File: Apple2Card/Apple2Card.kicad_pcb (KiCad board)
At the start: 2 copper layers, 160 x 78.2 mm, 77 parts, among them J1 ICSP, J2 Conn_01x25, J3 Conn_01x25, J4 Conn_01x16, J5 SERCON, J6 WIZNET 5500, SW1 SW_Push, U1 ATmega328P-P, U2 74HCT32, U3 74HCT00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

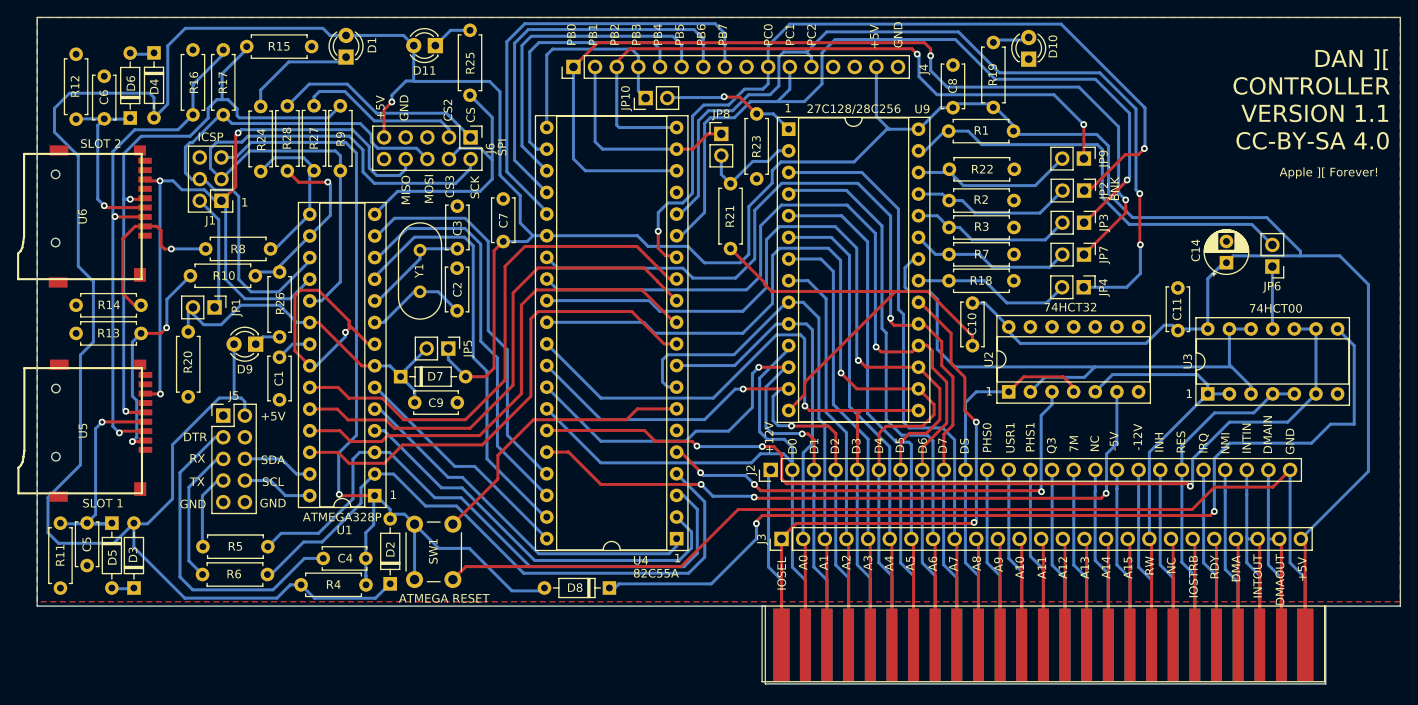
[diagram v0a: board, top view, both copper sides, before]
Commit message: Minor updates to PCB & schematics: - Realigned some components (LEDs etc). - Added some clearance to the slot connector (now allows production with "chamfered edges"). - Show component values on the silk screen (so no separate schematics are required when soldering) - Changed pull-down resistors for 82C55s I/O pins to 4k7 (instead of 10k), since they   were too weak to overcome the minimum current mentioned in the 8255 data sheet   (though the 10k resistors still worked with most types - but not with all). - Changed the two load resistors for the SD card supply voltage, to slightly increase the   voltage drop across the diodes. The SD supply voltage was a bit high.
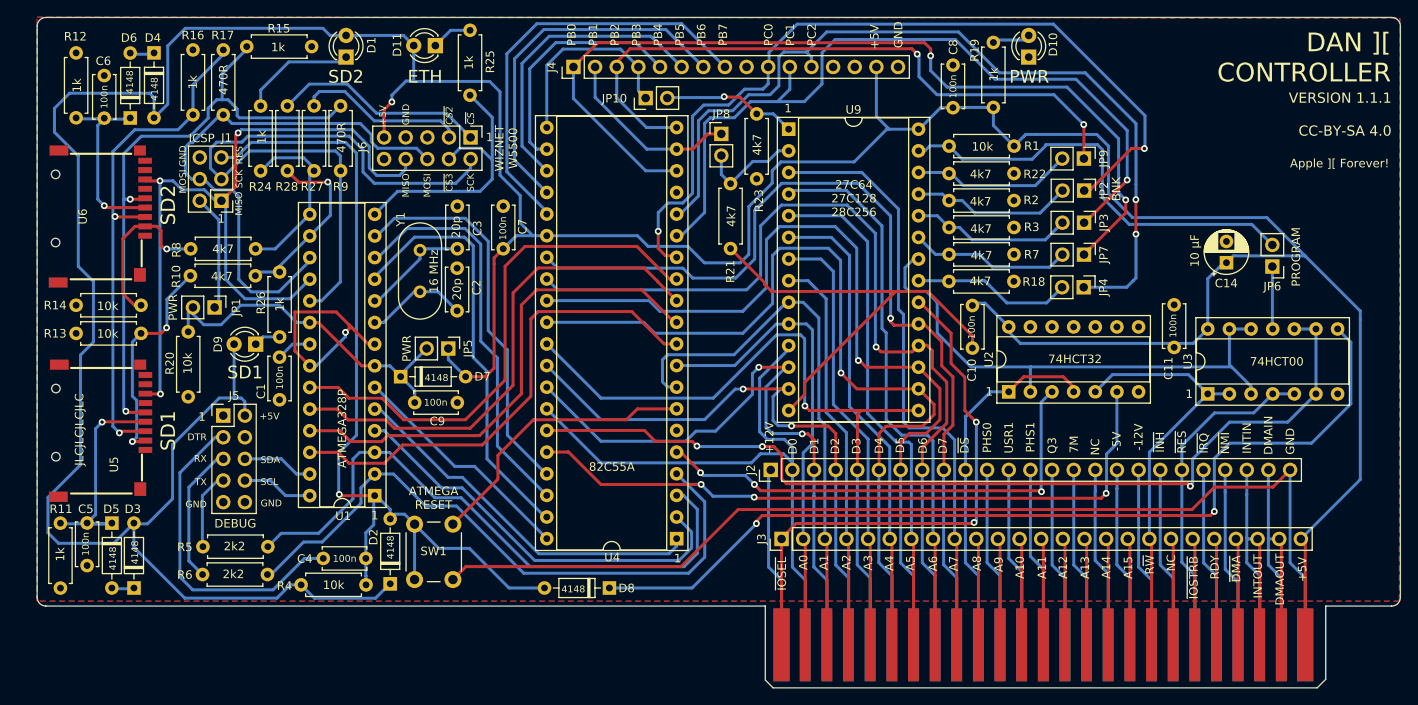
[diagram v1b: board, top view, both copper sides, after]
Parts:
- C1, C10, C11, C4, C5, C6, C7, C8, C9: value 100 nF -> 100n
- C14: value 10 uF -> 10 µF
- C2, C3: value 20 pF -> 20p
- D2, D3, D4, D5, D6, D7, D8: value 1N4148 -> 4148
- JP10: value PG2 -> PG9
- JP8: value PG2 -> PG4
- R11, R12: value 10k -> 1k
- U5: footprint Apple2Card:GCT-MEM2055-00-190-01-A -> Apple2Card:MicroSD_Card_TB
- moved C11 2.03 mm to (166.5, 64.1)
- moved R1 1.76 mm to (147.7, 40.5)
- moved R8 1.76 mm to (58.7, 52.6)
- moved C7 0.85 mm to (87.7, 52.5)
- moved R22 0.50 mm to (140.1, 43.7)
- moved C10 0.28 mm to (142.8, 59.2)
- moved D10 0.24 mm to (149.4, 30.1)
- moved R12 0.16 mm to (37.6, 29.6)
- moved C6 0.08 mm to (40.9, 37.2)
- moved R18 0.07 mm to (140.1, 56.4)
- moved R24 0.06 mm to (59.2, 35.8)
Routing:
- net Net-(U2-Pad2): track 70.0 -> 62.8 mm
- net PB0: track 111.6 -> 106.6 mm
- net Net-(J4-Pad8): track 53.1 -> 49.9 mm
- net PB1: track 24.7 -> 21.6 mm
- net Net-(J4-Pad7): track 45.6 -> 42.6 mm
- net Net-(D8-Pad1): track 112.2 -> 109.2 mm
- net Net-(J4-Pad6): track 38.1 -> 35.4 mm
- net Net-(J4-Pad5): track 31.1 -> 28.7 mm
- net GND: track 240.7 -> 238.4 mm
- net +5V: track 484.3 -> 482.0 mm
- net Net-(R14-Pad1): track 21.6 -> 19.5 mm
- net PB2: track 79.1 -> 77.3 mm
- net CS2: track 19.3 -> 21.1 mm
- net PC1: track 94.3 -> 92.8 mm
- net PB3: track 25.2 -> 23.7 mm
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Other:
- board size 160 x 78.2 mm -> 160 x 78.7 mm
- board text added: "27C64 27C128 28C256"
- board text added: "DAN ][ CONTROLLER"
- board text added: "DEBUG"
- board text added: "ETH"
- board text added: "JLCJLCJLCJLC"
- board text added: "PWR"
- board text added: "R~{W}"
- board text added: "SD1"
- board text added: "SD2"
- board text added: "VERSION 1.1.1 CC-BY-SA 4.0"
- board text added: "WIZNET W5500"
- board text added: "~{CS2}"
- board text added: "~{CS3}"
- board text added: "~{CS}"
- board text added: "~{DMA}"
- board text added: "~{DS}"
- board text added: "~{INH}"
- board text added: "~{IOSEL}"
- board text added: "~{IOSTRB}"
- board text added: "~{IRQ}"
- board text added: "~{NMI}"
- board text added: "~{RES}"
- board text removed: "27C128/28C256"
- board text removed: "CS"
- board text removed: "CS2"
- board text removed: "CS3"
- board text removed: "DAN ][ CONTROLLER VERSION 1.1 CC-BY-SA 4.0"
- board text removed: "DMA"
- board text removed: "DS"
- board text removed: "INH"
- board text removed: "IOSEL"
- board text removed: "IOSTRB"
- board text removed: "IRQ"
- board text removed: "NMI"
- board text removed: "RW"
- board text removed: "SLOT 1"
- board text removed: "SLOT 2"
- board text removed: "SPI"

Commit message: Documentation updates Matched name of ATmega328 Gerber file and link in README. Adapted links in README to use relative paths. Updated PCB image. Incorporated Dan's comment concerning D7/R20: they are optional. It's recommended to close JP5, in which case D7/R20 are obsolete.
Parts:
- R11, R12: value 1k -> 10k
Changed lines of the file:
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@@
     (property "Sheetfile" "Apple2Card.kicad_sch")
     (property "Sheetname" "")
-    (attr through_hole)
+    (attr through_hole exclude_from_bom)
     (fp_text reference "D7" (at 9.608 0) (layer "F.SilkS")
       (effects (font (size 1 1) (thickness 0.15)))
     )
-    (fp_text value "4148" (at 4.208 0.136) (layer "F.SilkS")
+    (fp_text value "4148" (at 4.208 0.136) (layer "F.SilkS") hide
       (effects (font (size 0.8 0.8) (thickness 0.1)))
     )
@@
     (pad "2" thru_hole oval (at 7.62 0) (size 1.6 1.6) (drill 0.8) (layers *.Cu *.Mask)
       (net 25 "+5V") (pinfunction "A") (pintype "passive"))
-    (model "${KICAD6_3DMODEL_DIR}/Diode_THT.3dshapes/D_DO-35_SOD27_P7.62mm_Horizontal.wrl"
+    (model "${KICAD6_3DMODEL_DIR}/Diode_THT.3dshapes/D_DO-35_SOD27_P7.62mm_Horizontal.wrl" hide
       (offset (xyz 0 0 0))
       (scale (xyz 1 1 1))
@@
       (effects (font (size 1 1) (thickness 0.15)))
     )
-    (fp_text value "1k" (at 3.81 -0.108 90) (layer "F.SilkS")
+    (fp_text value "10k" (at 3.81 -0.108 90) (layer "F.SilkS")
       (effects (font (size 1 1) (thickness 0.15)))
     )
@@
     (property "Sheetfile" "Apple2Card.kicad_sch")
     (property "Sheetname" "")
-    (attr through_hole)
+    (attr through_hole exclude_from_bom)
     (fp_text reference "R20" (at 3.92 -2.15 90) (layer "F.SilkS")
       (effects (font (size 1 1) (thickness 0.15)))
     )
-    (fp_text value "10k" (at 3.92 -0.05 90) (layer "F.SilkS")
+    (fp_text value "10k" (at 3.92 -0.05 90) (layer "F.SilkS") hide
       (effects (font (size 1 1) (thickness 0.15)))
     )
@@
     (pad "2" thru_hole oval (at 7.62 0 90) (size 1.6 1.6) (drill 0.8) (layers *.Cu *.Mask)
       (net 73 "Net-(C9-Pad1)") (pintype "passive"))
-    (model "${KICAD6_3DMODEL_DIR}/Resistor_THT.3dshapes/R_Axial_DIN0207_L6.3mm_D2.5mm_P7.62mm_Horizontal.wrl"
+    (model "${KICAD6_3DMODEL_DIR}/Resistor_THT.3dshapes/R_Axial_DIN0207_L6.3mm_D2.5mm_P7.62mm_Horizontal.wrl" hide
       (offset (xyz 0 0 0))
       (scale (xyz 1 1 1))
@@
       (effects (font (size 1 1) (thickness 0.15)))
     )
-    (fp_text value "1k" (at 3.9626 -0.0122 90) (layer "F.SilkS")
-      (effects (font (size 1 1) (thickness 0.15)))
-    )
+    (fp_text value "10k" (at 3.9626 -0.0122 90) (layer "F.SilkS")
+      (effects (font (size 1 1) (thickness 0.15)))
+    )
